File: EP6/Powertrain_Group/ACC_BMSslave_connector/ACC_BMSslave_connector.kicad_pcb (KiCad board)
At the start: 2 copper layers, 200 x 59 mm, 47 parts, among them J1 V11-14, J10 Conn_01x02_Pin, J11 Conn_01x02_Pin, J12 Conn_01x02_Pin, J13 Conn_01x02_Pin, J14 Conn_01x02_Pin, J15 Conn_01x02_Pin, J16 Conn_01x02_Pin, J17 Conn_01x02_Pin, J18 Conn_01x02_Pin, J19 Conn_01x02_Pin, J2 V7-10, J20 Conn_01x02_Pin, J21 Conn_01x02_Pin, J22 Conn_01x02_Pin, J23 Conn_01x02_Pin, J24 Conn_01x02_Pin, J25 Conn_01x02_Pin, J26 Conn_01x02_Pin, J27 Conn_01x02_Pin, J28 Conn_01x02_Pin, J29 Conn_01x02_Pin, J3 V3-6, J30 Conn_01x02_Pin, J31 Conn_01x02_Pin, J32 Conn_01x02_Pin, J33 Conn_01x02_Pin, J34 Conn_01x02_Pin, J35 Conn_01x02_Pin, J36 Conn_01x02_Pin, J37 B2B_CELL_TAPS_1, J38 B2B_NTC_1, J39 B2B_NTC_2, J4 V0-2, J40 B2B_CELL_TAPS_2, J41 B2B_NTC_3, J42 B2B_NTC_4, J43 B2B_DUMMY, J5 Conn_01x02_Pin, J6 Conn_01x02_Pin, J7 Conn_01x02_Pin, J8 Conn_01x02_Pin, J9 Conn_01x02_Pin

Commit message: [BMSslave_connector] board done
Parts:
- added ? (x4): , Graphics, F.Cu at (209.3, -24.8)
- added ?: , Graphics, B.Cu at (209.3, -22.5)
- added ? (x4): , Graphics, F.Cu at (209.3, -22.5)
- added ?: , Graphics, B.Cu at (209.3, -24.8)
- J1, J2, J3, J4: footprint Connector_JST:JST_XH_B4B-XH-A_1x04_P2.50mm_Vertical -> Connector_JST:JST_XH_S4B-XH-A_1x04_P2.50mm_Horizontal
- J10, J11, J12, J13, J14, J15, J16, J17, J18, J19, J20, J21, J22, J23, J24, J25, J26, J27, J28, J29, J30, J31, J32, J33, J34, J35, J36, J5, J6, J7, J8, J9: moved to F.Cu
- moved J14 176.3 mm to (235.8, 109.5), turned to 180 degrees
- moved J13 171.3 mm to (225.8, 109.5), turned to 180 degrees
- moved J9 169.7 mm to (58.8, 109.5), turned to 180 degrees
- moved J15 166.4 mm to (230.8, 102.5), turned to 180 degrees
- moved J10 164.7 mm to (68.8, 109.5), turned to 180 degrees
- moved J11 159.7 mm to (78.8, 109.5), turned to 180 degrees
- moved J12 154.7 mm to (88.8, 109.5), turned to 180 degrees
- moved J16 151.4 mm to (220.8, 102.5), turned to 180 degrees
- moved J29 99.9 mm to (187.2, 60.0), turned to 0 degrees
- moved J30 94.9 mm to (177.2, 60.0), turned to 0 degrees
- moved J31 89.9 mm to (167.2, 60.0), turned to 0 degrees
- moved J32 84.9 mm to (157.2, 60.0), turned to 0 degrees
- moved J28 69.2 mm to (60.2, 64.5), turned to 0 degrees
- moved J27 64.2 mm to (70.2, 64.5), turned to 0 degrees
- moved J26 59.2 mm to (80.2, 64.5), turned to 0 degrees
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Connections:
- net Net-(J1-Pin_1) renamed /CT15
- net Net-(J1-Pin_2) renamed /CT14
- net Net-(J1-Pin_3) renamed /CT13
- net Net-(J1-Pin_4) renamed /CT12
- net Net-(J2-Pin_1) renamed /CT11
- net Net-(J2-Pin_2) renamed /CT10
- net Net-(J2-Pin_3) renamed /CT9
- net Net-(J2-Pin_4) renamed /CT8
- net Net-(J3-Pin_1) renamed /CT7
- net Net-(J3-Pin_2) renamed /CT6
- net Net-(J3-Pin_3) renamed /CT5
- net Net-(J3-Pin_4) renamed /CT4
- net Net-(J37-Pin_1) renamed /CT0
- net Net-(J37-Pin_2) renamed /CT1
- net Net-(J37-Pin_3) renamed /CT2
- net Net-(J37-Pin_4) renamed /CT3
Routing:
- net /CT0: track 0.00 -> 116.6 mm
- net /CT1: track 0.00 -> 113.2 mm
- net /CT2: track 0.00 -> 110.3 mm
- net /CT3: track 0.00 -> 106.9 mm
- net T8: track 147.5 -> 41.5 mm
- net T9: track 137.9 -> 55.6 mm
- net T25: track 113.8 -> 38.4 mm
- net T24: track 111.3 -> 36.5 mm
- net T26: track 113.7 -> 40.5 mm
- net T27: track 116.2 -> 43.6 mm
- net T23: track 47.8 -> 120.3 mm
- net T10: track 125.6 -> 55.1 mm
- net T11: track 115.9 -> 47.6 mm
- net T22: track 46.8 -> 112.9 mm
- net T21: track 46.8 -> 108.0 mm
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- added copper zone on In1.Cu, net Earth
- added copper zone on In2.Cu, net Earth
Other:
- board size 200 x 59 mm -> 200 x 56 mm
- copper layers 2 -> 4
- board text added: "BMSslave_connector"
- board text added: "CT0"
- board text added: "CT1"
- board text added: "CT10"
- board text added: "CT11"
- board text added: "CT12"
- board text added: "CT13"
- board text added: "CT14"
- board text added: "CT15"
- board text added: "CT2"
- board text added: "CT3"
- board text added: "CT4"
- board text added: "CT5"
- board text added: "CT6"
- board text added: "CT7"
- board text added: "CT8"
- board text added: "CT9"
- board text added: "EP6"
- board text added: "T0"
- board text added: "T1"
- board text added: "T10"
- board text added: "T11"
- board text added: "T12"
- board text added: "T13"
- board text added: "T14"
- board text added: "T15"
- board text added: "T16"
- board text added: "T17"
- board text added: "T18"
- board text added: "T19"
- board text added: "T2"
- board text added: "T20"
- board text added: "T21"
- board text added: "T22"
- board text added: "T23"
- board text added: "T24"
- board text added: "T25"
- board text added: "T26"
- board text added: "T27"
- board text added: "T28"
- board text added: "T29"
- board text added: "T3"
- board text added: "T30"
- board text added: "T31"
- board text added: "T4"
- board text added: "T5"
- board text added: "T6"
- board text added: "T7"
- board text added: "T8"
- board text added: "T9"
- board text added: "jerrymk 20250307"

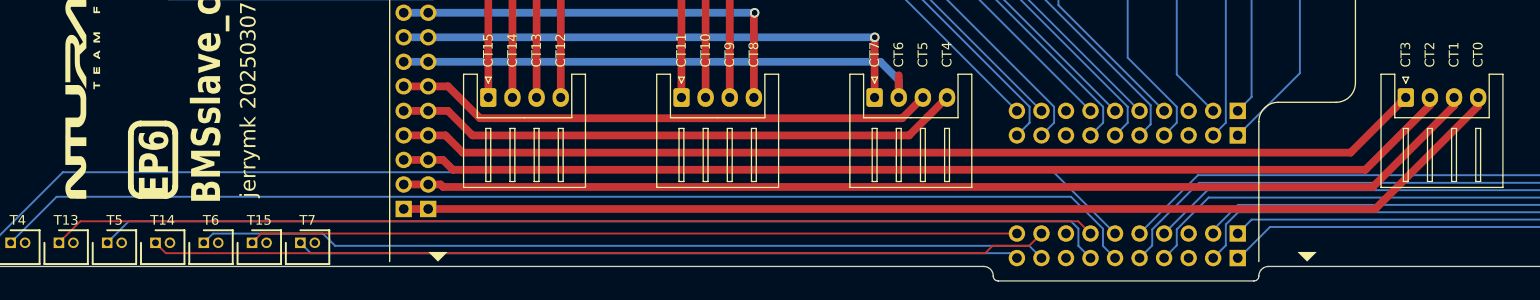
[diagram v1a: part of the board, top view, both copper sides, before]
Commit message: [BMSslave_connector] slight adjustment
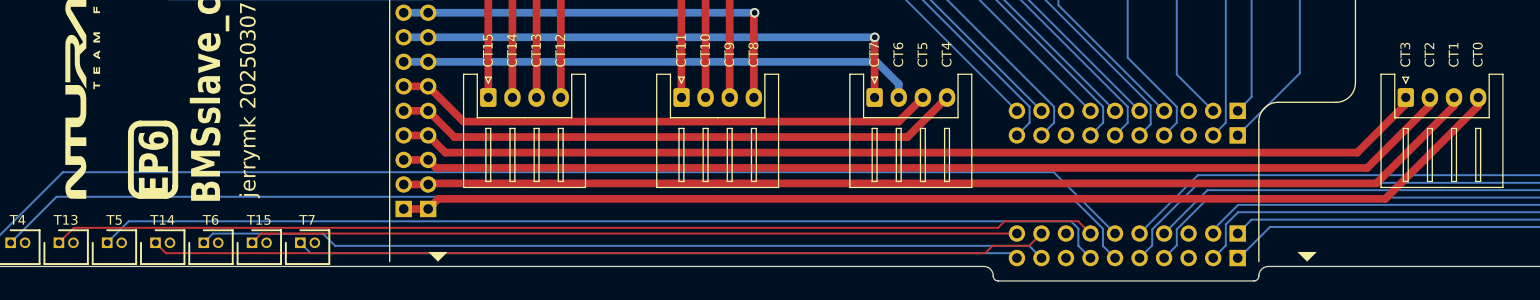
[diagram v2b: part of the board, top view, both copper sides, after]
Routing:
- net /CT6: track 56.2 -> 53.6 mm

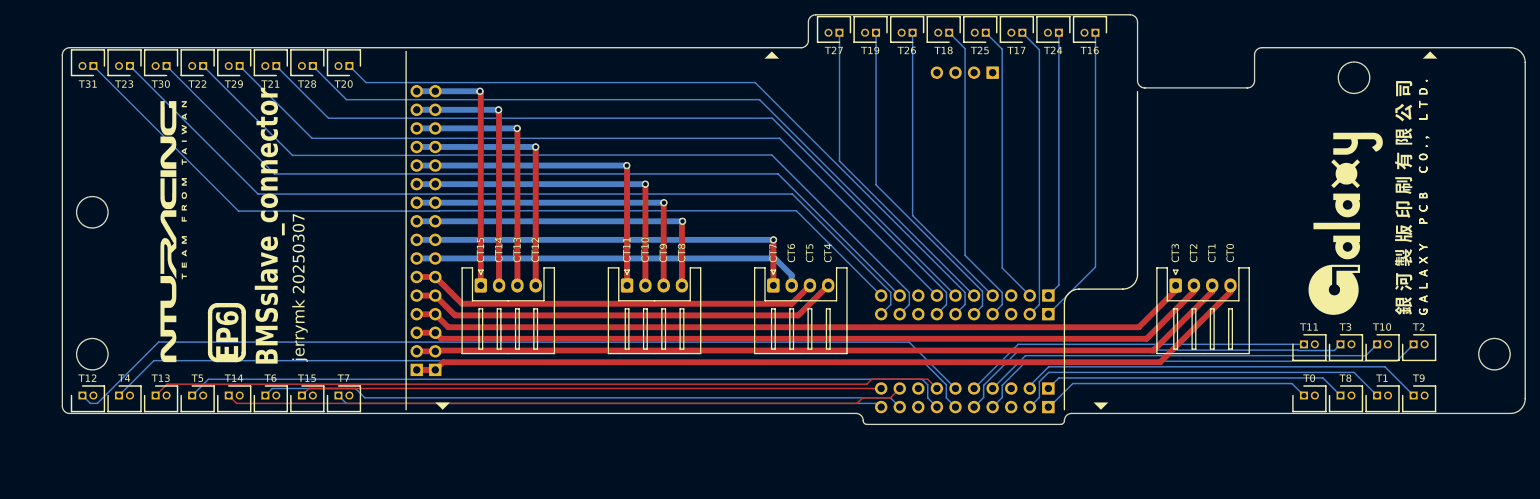
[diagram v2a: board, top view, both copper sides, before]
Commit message: [BMSslave_connector] adjust silk and changed tracks
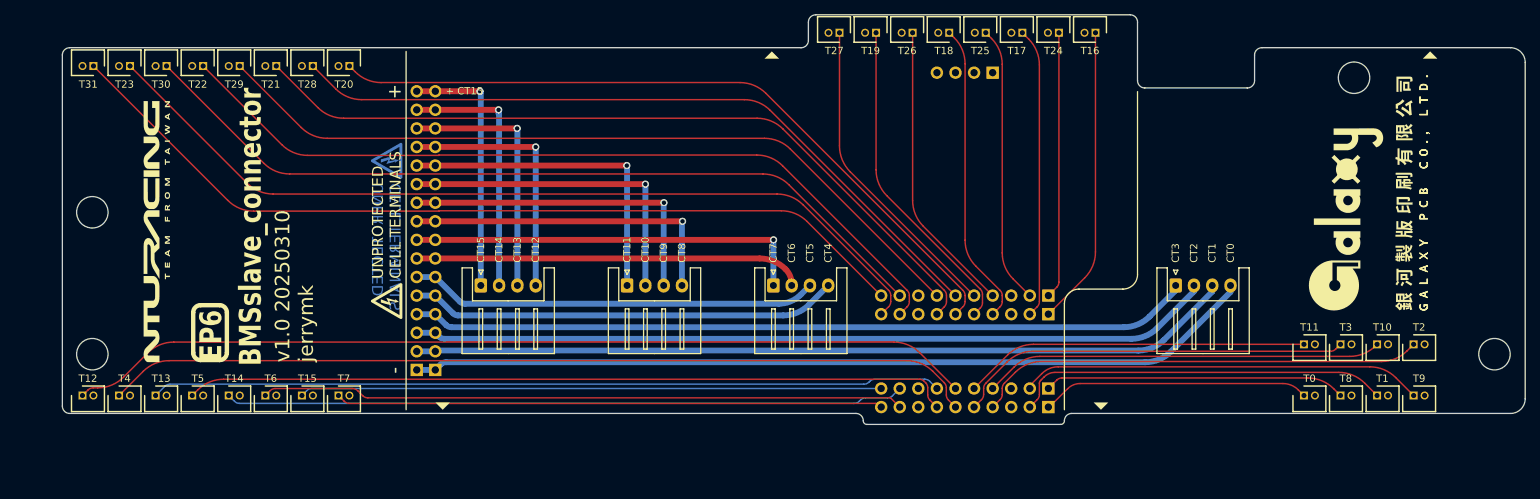
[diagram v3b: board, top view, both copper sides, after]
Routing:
- net T12: track 125.9 -> 124.2 mm
- net T9: track 55.6 -> 54.8 mm
- net T10: track 55.1 -> 54.3 mm
- net T4: track 120.0 -> 119.4 mm
- net T22: track 112.9 -> 112.3 mm
- net T20: track 100.5 -> 99.9 mm
- net T2: track 62.1 -> 61.5 mm
- net T18: track 42.0 -> 41.4 mm
- net T23: track 120.3 -> 119.8 mm
- net T21: track 108.0 -> 107.4 mm
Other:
- board text added: "+"
- board text added: "+ CT15"
- board text added: "-"
- board text added: "UNPROTECTED CELL TERMINALS"
- board text added: "v1.0 20250310 jerrymk"
- board text removed: "jerrymk 20250307"

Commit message: [BMSslave_connector] v1.1, move mounting holes
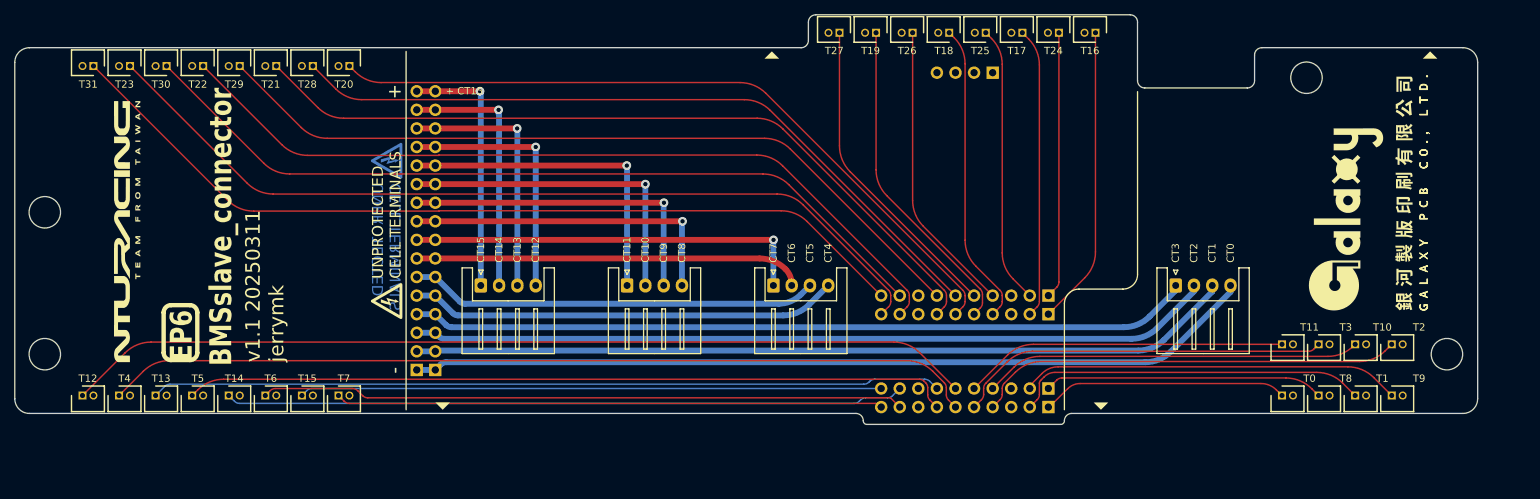
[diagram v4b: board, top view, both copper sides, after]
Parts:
- J37, J40: footprint Connector_PinHeader_2.54mm:PinHeader_1x16_P2.54mm_Vertical -> Connector_PinSocket_2.54mm:PinSocket_1x16_P2.54mm_Vertical
- J38, J39, J41, J42: footprint Connector_PinHeader_2.54mm:PinHeader_1x10_P2.54mm_Vertical -> Connector_PinSocket_2.54mm:PinSocket_1x10_P2.54mm_Vertical
- J43: footprint Connector_PinHeader_2.54mm:PinHeader_1x04_P2.54mm_Vertical -> Connector_PinSocket_2.54mm:PinSocket_1x04_P2.54mm_Vertical
- moved H1 6.50 mm to (48.6, 103.9)
- moved H2 6.50 mm to (48.6, 84.5)
- moved H3 6.50 mm to (221.1, 66.1)
- moved H4 6.50 mm to (240.3, 103.9)
- moved J13 3.00 mm to (222.8, 109.5)
- moved J14 3.00 mm to (232.8, 109.5)
- moved J15 3.00 mm to (227.8, 102.5)
- moved J16 3.00 mm to (217.8, 102.5)
- moved J5 3.00 mm to (217.8, 109.5)
- moved J6 3.00 mm to (227.8, 109.5)
- moved J7 3.00 mm to (232.8, 102.5)
- moved J8 3.00 mm to (222.8, 102.5)
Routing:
- net T9: track 54.8 -> 51.8 mm
- net T8: track 41.2 -> 38.2 mm
- net T3: track 54.2 -> 51.2 mm
- net T2: track 61.5 -> 58.5 mm
- net T11: track 47.4 -> 44.4 mm
- net T10: track 54.3 -> 51.3 mm
- net T1: track 51.6 -> 48.6 mm
- net T0: track 36.6 -> 33.6 mm
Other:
- outline, holes or cut-outs redrawn
- board text added: "v1.1 20250311 jerrymk"
- board text removed: "v1.0 20250310 jerrymk"
